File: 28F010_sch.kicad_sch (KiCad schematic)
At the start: 13 parts, among them U10 74LVC1G332, U11 74LS138, U12 CY7C199, U13 74LS14, U14 74LS14, U15 CY7C199, U16 4012, U17 CY7C199, U7 74LS13, U8 74LS138, U9 CY7C199

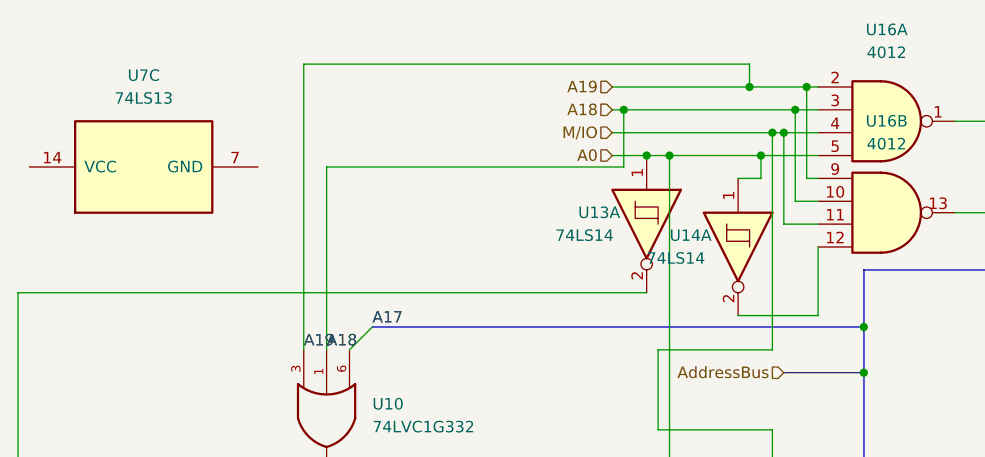
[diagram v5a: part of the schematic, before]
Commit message: Wired up Decoding of 8255s, 8254, and 8279
Also fixed up the decoding for the 16550 and the 8259 as well as labeled all wires into/from the bus.
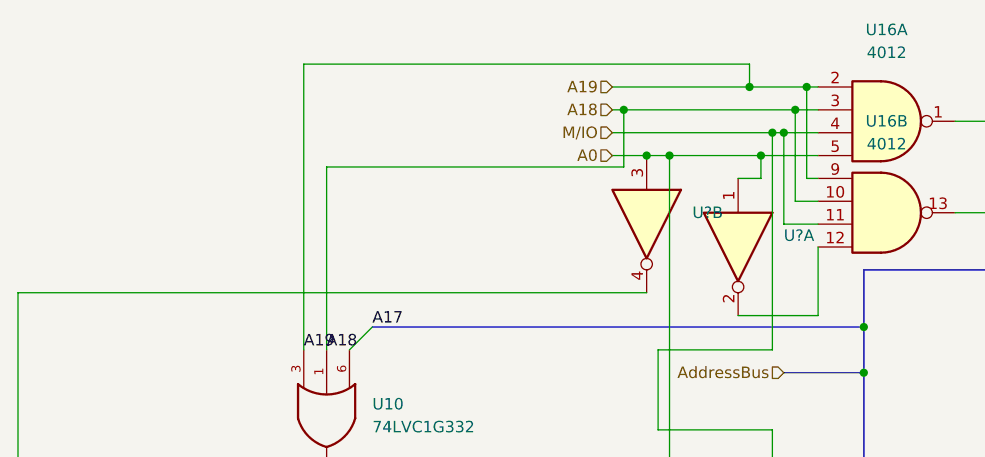
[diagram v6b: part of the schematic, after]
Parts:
- removed U13, U14: 74LS14, symbol 74xx:74LS14
- removed U7: 74LS13, symbol 74xx:74LS13
- added U? (x2): (no value), symbol 74xx:74LS04
- Bank0, Bank1: footprint (none) -> parts:28F010
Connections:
- net A0: now also U?.1, U?.3, U?.4
- net at U16.12: now also U?.2
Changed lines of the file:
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@@
   (junction (at 257.81 50.8) (diameter 0) (color 0 0 0 0)
   )
+  (junction (at 99.06 20.32) (diameter 0) (color 0 0 0 0)
+  )
+  (junction (at 54.61 114.3) (diameter 0) (color 0 0 0 0)
+  )
+  (junction (at 96.52 15.24) (diameter 0) (color 0 0 0 0)
+  )
+  (junction (at 55.88 60.96) (diameter 0) (color 0 0 0 0)
+  )
+  (junction (at 93.98 114.3) (diameter 0) (color 0 0 0 0)
+  )
+  (junction (at 82.55 17.78) (diameter 0) (color 0 0 0 0)
+  )
+  (junction (at 100.33 20.32) (diameter 0) (color 0 0 0 0)
+  )
+  (junction (at 49.53 59.69) (diameter 0) (color 0 0 0 0)
+  )
+  (junction (at 109.22 46.99) (diameter 0) (color 0 0 0 0)
+  )
+  (junction (at 109.22 99.06) (diameter 0) (color 0 0 0 0)
+  )
   (junction (at 85.09 22.86) (diameter 0) (color 0 0 0 0)
   )
-  (junction (at 99.06 20.32) (diameter 0) (color 0 0 0 0)
-  )
-  (junction (at 54.61 114.3) (diameter 0) (color 0 0 0 0)
-  )
-  (junction (at 96.52 15.24) (diameter 0) (color 0 0 0 0)
-  )
-  (junction (at 55.88 60.96) (diameter 0) (color 0 0 0 0)
-  )
-  (junction (at 93.98 114.3) (diameter 0) (color 0 0 0 0)
-  )
-  (junction (at 82.55 17.78) (diameter 0) (color 0 0 0 0)
-  )
-  (junction (at 100.33 20.32) (diameter 0) (color 0 0 0 0)
-  )
-  (junction (at 49.53 59.69) (diameter 0) (color 0 0 0 0)
-  )
-  (junction (at 109.22 46.99) (diameter 0) (color 0 0 0 0)
-  )
-  (junction (at 109.22 99.06) (diameter 0) (color 0 0 0 0)
-  )
   (junction (at 101.6 17.78) (diameter 0) (color 0 0 0 0)
   )
@@
     (stroke (width 0) (type default) (color 0 0 0 0))
   )
+  (wire (pts (xy 85.09 22.86) (xy 87.63 22.86))
+    (stroke (width 0) (type default) (color 0 0 0 0))
+  )
   (wire (pts (xy 95.25 40.64) (xy 104.14 40.64))
     (stroke (width 0) (type default) (color 0 0 0 0))
@@
   )
   (bus (pts (xy 54.61 171.45) (xy 54.61 173.99))
-    (stroke (width 0) (type default) (color 0 0 0 0))
-  )
-  (wire (pts (xy 85.09 22.86) (xy 87.63 22.86))
     (stroke (width 0) (type default) (color 0 0 0 0))
   )
@@
   (hierarchical_label "AddressBus" (shape input) (at 100.33 46.99 180)
     (effects (font (size 1.27 1.27)) (justify right))
+  )
+  (symbol (lib_id "74xx:74LS04") (at 85.09 30.48 270) (unit 2)
+    (in_bom yes) (on_board yes) (fields_autoplaced)
+    (property "Reference" "U?" (id 0) (at 90.17 29.2099 90)
+      (effects (font (size 1.27 1.27)) (justify left))
+    )
+    (property "Value" "" (id 1) (at 90.17 31.7499 90)
+      (effects (font (size 1.27 1.27)) (justify left))
+    )
+    (property "Footprint" "" (id 2) (at 85.09 30.48 0)
+      (effects (font (size 1.27 1.27)) hide)
+    )
+    (property "Datasheet" "http://www.ti.com/lit/gpn/sn74LS04" (id 3) (at 85.09 30.48 0)
+      (effects (font (size 1.27 1.27)) hide)
+    )
+    (pin "1")
+    (pin "2")
+    (pin "3")
+    (pin "4")
+    (pin "5")
+    (pin "6")
+    (pin "8")
+    (pin "9")
+    (pin "10")
+    (pin "11")
+    (pin "12")
+    (pin "13")
+    (pin "14")
+    (pin "7")
   )
   (symbol (lib_id "28F010:28F010") (at 182.88 93.98 0) (unit 1)
@@
       (effects (font (size 1.524 1.524)))
     )
-    (property "Footprint" "" (id 2) (at 210.82 87.884 0)
+    (property "Footprint" "parts:28F010" (id 2) (at 210.82 87.884 0)
       (effects (font (size 1.524 1.524)) hide)
     )
@@
     (pin "9")
   )
-  (symbol (lib_id "74xx:74LS13") (at 29.21 24.13 90) (unit 3)
-    (in_bom yes) (on_board yes) (fields_autoplaced)
-    (property "Reference" "U7" (id 0) (at 29.21 13.97 90))
-    (property "Value" "74LS13" (id 1) (at 29.21 16.51 90))
-    (property "Footprint" "" (id 2) (at 29.21 24.13 0)
-      (effects (font (size 1.27 1.27)) hide)
-    )
-    (property "Datasheet" "http://www.ti.com/lit/gpn/sn74LS13" (id 3) (at 29.21 24.13 0)
-      (effects (font (size 1.27 1.27)) hide)
-    )
-    (pin "1")
-    (pin "2")
-    (pin "4")
-    (pin "5")
-    (pin "6")
-    (pin "10")
-    (pin "12")
-    (pin "13")
-    (pin "8")
-    (pin "9")
-    (pin "14")
-    (pin "7")
-  )
   (symbol (lib_id "74xx:74LS138") (at 72.39 82.55 0) (unit 1)
     (in_bom yes) (on_board yes) (fields_autoplaced)
@@
     (pin "9")
   )
-  (symbol (lib_id "74xx:74LS14") (at 85.09 30.48 270) (unit 1)
-    (in_bom yes) (on_board yes)
-    (property "Reference" "U13" (id 0) (at 77.47 29.21 90)
+  (symbol (lib_id "4xxx:4012") (at 111.76 19.05 0) (unit 1)
+    (in_bom yes) (on_board yes) (fields_autoplaced)
+    (property "Reference" "U16" (id 0) (at 111.76 8.89 0))
+    (property "Value" "4012" (id 1) (at 111.76 11.43 0))
+    (property "Footprint" "" (id 2) (at 111.76 19.05 0)
+      (effects (font (size 1.27 1.27)) hide)
+    )
+    (property "Datasheet" "http://www.intersil.com/content/dam/Intersil/documents/cd40/cd4011bms-12bms-23bms.pdf" (id 3) (at 111.76 19.05 0)
+      (effects (font (size 1.27 1.27)) hide)
+    )
+    (pin "1")
+    (pin "2")
+    (pin "3")
+    (pin "4")
+    (pin "5")
+    (pin "10")
+    (pin "11")
+    (pin "12")
+    (pin "13")
+    (pin "9")
+    (pin "14")
+    (pin "7")
+  )
+  (symbol (lib_id "74xx:74LS04") (at 95.25 33.02 270) (unit 1)
+    (in_bom yes) (on_board yes) (fields_autoplaced)
+    (property "Reference" "U?" (id 0) (at 100.33 31.7499 90)
       (effects (font (size 1.27 1.27)) (justify left))
     )
-    (property "Value" "74LS14" (id 1) (at 74.93 31.75 90)
+    (property "Value" "" (id 1) (at 100.33 34.2899 90)
       (effects (font (size 1.27 1.27)) (justify left))
     )
-    (property "Footprint" "" (id 2) (at 85.09 30.48 0)
+    (property "Footprint" "" (id 2) (at 95.25 33.02 0)
       (effects (font (size 1.27 1.27)) hide)
     )
-    (property "Datasheet" "http://www.ti.com/lit/gpn/sn74LS14" (id 3) (at 85.09 30.48 0)
+    (property "Datasheet" "http://www.ti.com/lit/gpn/sn74LS04" (id 3) (at 95.25 33.02 0)
       (effects (font (size 1.27 1.27)) hide)
     )
@@
     (pin "12")
     (pin "13")
-    (pin "14")
-    (pin "7")
-  )
-  (symbol (lib_id "4xxx:4012") (at 111.76 19.05 0) (unit 1)
-    (in_bom yes) (on_board yes) (fields_autoplaced)
-    (property "Reference" "U16" (id 0) (at 111.76 8.89 0))
-    (property "Value" "4012" (id 1) (at 111.76 11.43 0))
-    (property "Footprint" "" (id 2) (at 111.76 19.05 0)
-      (effects (font (size 1.27 1.27)) hide)
-    )
-    (property "Datasheet" "http://www.intersil.com/content/dam/Intersil/documents/cd40/cd4011bms-12bms-23bms.pdf" (id 3) (at 111.76 19.05 0)
-      (effects (font (size 1.27 1.27)) hide)
-    )
-    (pin "1")
-    (pin "2")
-    (pin "3")
-    (pin "4")
-    (pin "5")
-    (pin "10")
-    (pin "11")
-    (pin "12")
-    (pin "13")
-    (pin "9")
     (pin "14")
     (pin "7")
@@
     (pin "9")
   )
-  (symbol (lib_id "74xx:74LS14") (at 95.25 33.02 270) (unit 1)
-    (in_bom yes) (on_board yes)
-    (property "Reference" "U14" (id 0) (at 87.63 31.75 90)
-      (effects (font (size 1.27 1.27)) (justify left))
-    )
-    (property "Value" "74LS14" (id 1) (at 85.09 34.29 90)
-      (effects (font (size 1.27 1.27)) (justify left))
-    )
-    (property "Footprint" "" (id 2) (at 95.25 33.02 0)
-      (effects (font (size 1.27 1.27)) hide)
-    )
-    (property "Datasheet" "http://www.ti.com/lit/gpn/sn74LS14" (id 3) (at 95.25 33.02 0)
-      (effects (font (size 1.27 1.27)) hide)
-    )
-    (pin "1")
-    (pin "2")
-    (pin "3")
-    (pin "4")
-    (pin "5")
-    (pin "6")
-    (pin "8")
-    (pin "9")
-    (pin "10")
-    (pin "11")
-    (pin "12")
-    (pin "13")
-    (pin "14")
-    (pin "7")
-  )
   (symbol (lib_id "28F010:28F010") (at 181.61 30.48 0) (unit 1)
     (in_bom yes) (on_board yes) (fields_autoplaced)
@@
       (effects (font (size 1.524 1.524)))
     )
-    (property "Footprint" "" (id 2) (at 209.55 24.384 0)
+    (property "Footprint" "parts:28F010" (id 2) (at 209.55 24.384 0)
       (effects (font (size 1.524 1.524)) hide)
     )

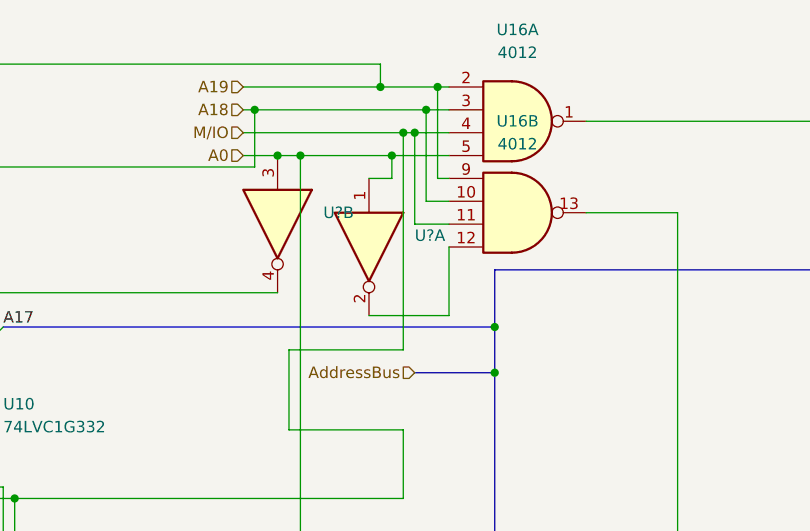
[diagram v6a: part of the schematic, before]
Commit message: Wired the max235 and DSUB9
We will double check the wiring tomorrow. Also added the data bus
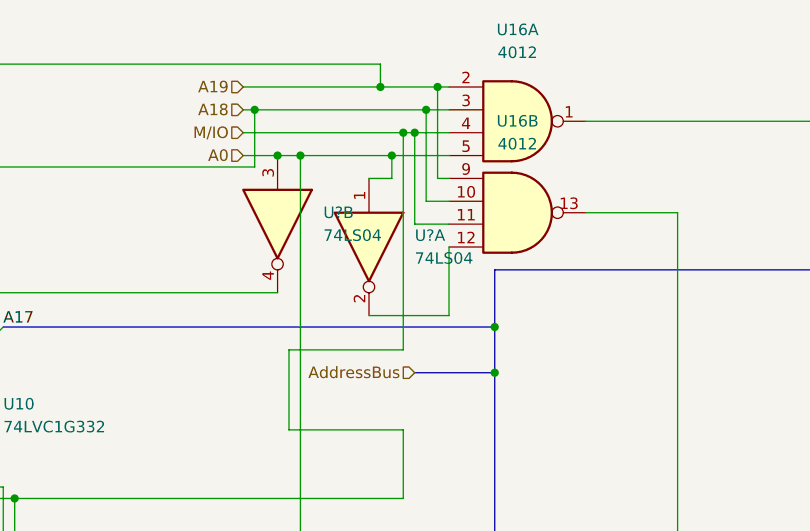
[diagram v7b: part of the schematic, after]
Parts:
- U? (x2): value (none) -> 74LS04
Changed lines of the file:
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@@
       (effects (font (size 1.27 1.27)) (justify left))
     )
-    (property "Value" "" (id 1) (at 90.17 31.7499 90)
+    (property "Value" "74LS04" (id 1) (at 90.17 31.7499 90)
       (effects (font (size 1.27 1.27)) (justify left))
     )
@@
       (effects (font (size 1.27 1.27)) (justify left))
     )
-    (property "Value" "" (id 1) (at 100.33 34.2899 90)
-      (effects (font (size 1.27 1.27)) (justify left))
-    )
+    (property "Value" "74LS04" (id 1) (at 100.33 34.2899 90)
+      (effects (font (size 1.27 1.27)) (justify left))
+    )

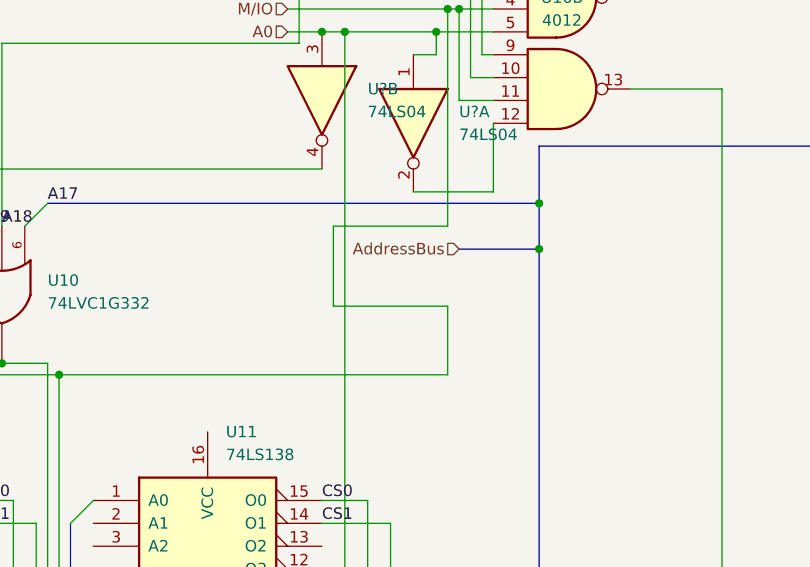
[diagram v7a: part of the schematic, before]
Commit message: Added Clock Circuit
Moved the main circuit to the right and added a simple clock generator circuit to the left of the 8086. Still need to wire reset switch
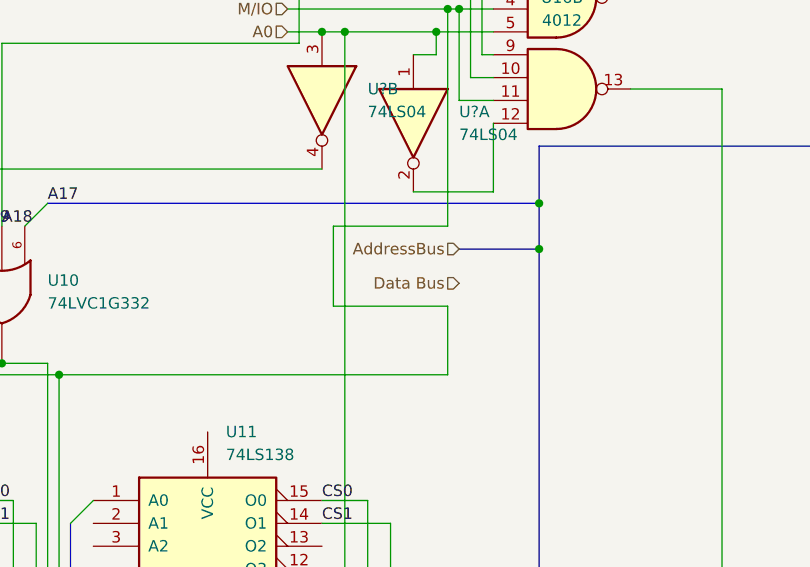
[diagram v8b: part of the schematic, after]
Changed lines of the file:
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@@
+    (effects (font (size 1.27 1.27)) (justify right))
+  )
+  (hierarchical_label "Data Bus" (shape input) (at 100.33 50.8 180)
     (effects (font (size 1.27 1.27)) (justify right))
   )
